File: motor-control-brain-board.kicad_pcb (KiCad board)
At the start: 2 copper layers, 107 parts, among them J1 GPIO, J10 PWM, J11 PWR, J12 POWER_SENSE, J13 MISC_SENSE, J2 I2C, J3 SERIAL_1, J4 SERIAL_2, J5 CAN, J6 SPI, J7 USB_C_Receptacle_USB2.0_16P, J8 SWD, J9 POS_SENSE, SW1 RST, U1 TLV76750QWDRBxQ1, U10 TLV6001DCK, U11 TLV6001DCK, U12 TLV6001DCK, U2 TLV76733QWDRBxQ1, U3 M95256-WMN6P, U4 STM32G474RETx, U5 TCAN1044V-Q1, U6 TLV6001DCK, U7 TLV6001DCK, U8 TLV6001DCK, U9 TLV6001DCK

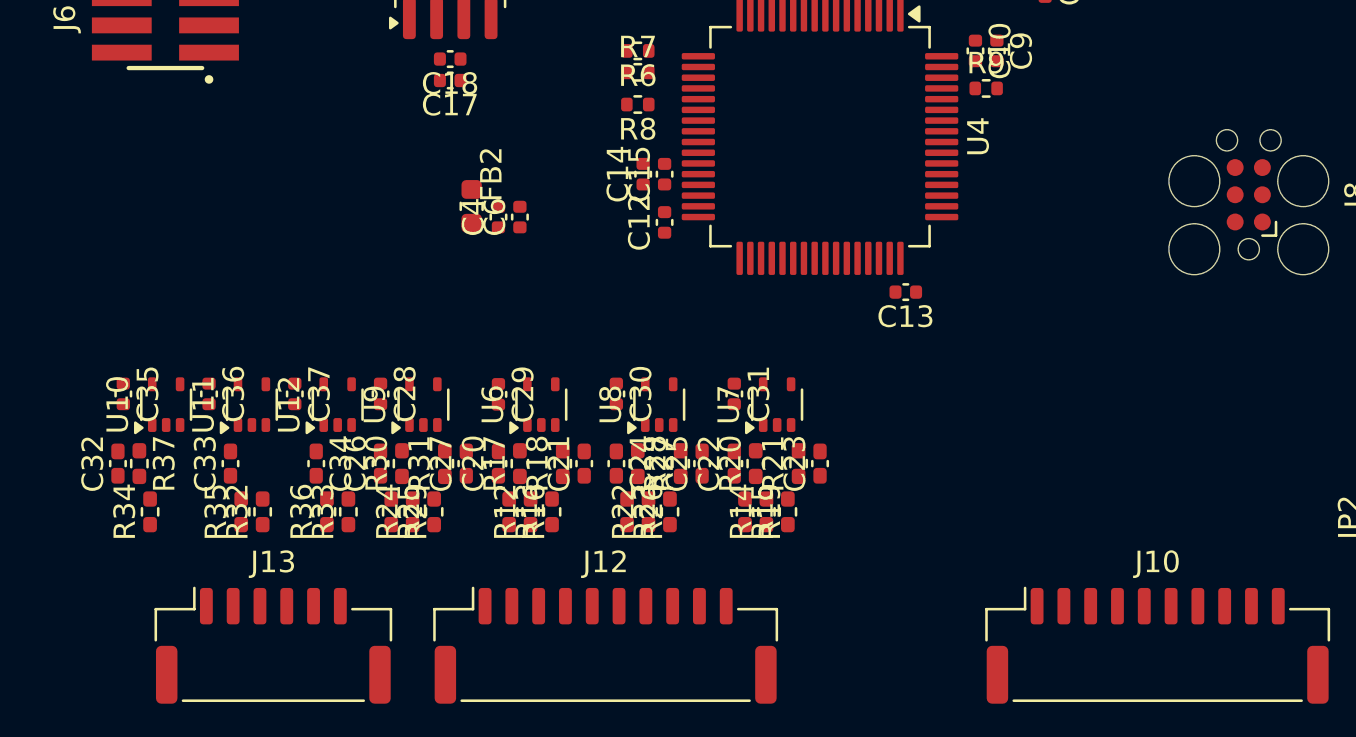
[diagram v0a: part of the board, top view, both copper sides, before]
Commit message: Started routing PCB
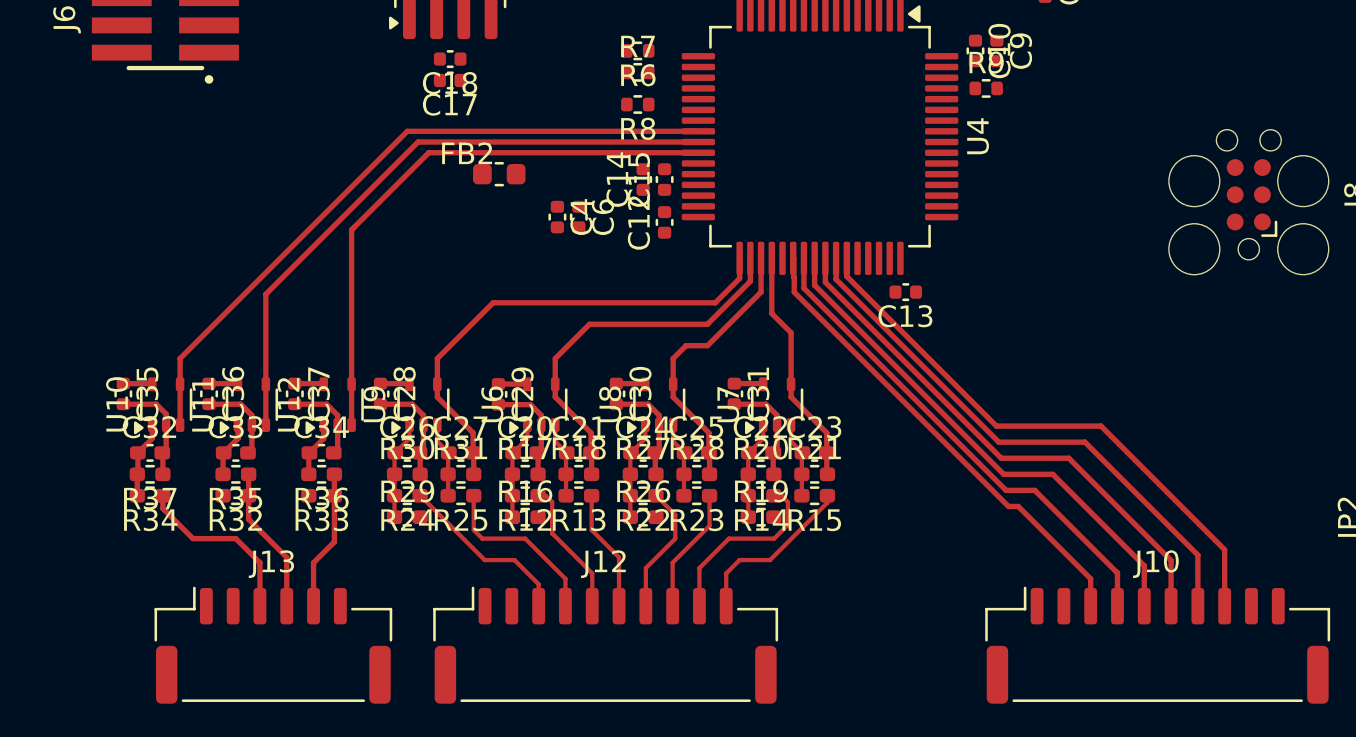
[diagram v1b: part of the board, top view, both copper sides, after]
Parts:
- C19: value C -> 4n7
- moved C4 2.75 mm to (128.0, 102.0), turned to -90 degrees
- moved C6 2.75 mm to (129.0, 102.0), turned to -90 degrees
- moved FB2 1.98 mm to (125.3, 100.0), turned to 0 degrees
- moved R35 1.77 mm to (113.0, 114.0), turned to 180 degrees
- moved R36 1.77 mm to (117.0, 114.0), turned to 180 degrees
- moved C32 1.58 mm to (109.0, 113.0), turned to 0 degrees
- moved R13 1.46 mm to (129.0, 115.0), turned to 180 degrees
- moved R15 1.46 mm to (140.0, 115.0), turned to 180 degrees
- moved R23 1.46 mm to (134.5, 115.0), turned to 180 degrees
- moved R25 1.46 mm to (123.5, 115.0), turned to 180 degrees
- moved R32 1.46 mm to (113.0, 115.0), turned to 180 degrees
- moved R33 1.46 mm to (117.0, 115.0), turned to 180 degrees
- moved C20 1.35 mm to (126.5, 113.0), turned to 0 degrees
- moved C22 1.35 mm to (137.5, 113.0), turned to 0 degrees
- moved C24 1.35 mm to (132.0, 113.0), turned to 0 degrees
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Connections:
- J1 pad 10: /GPIO_7 -> GND
- J1 pad 3: GND -> /GPIO_1
- J1 pad 4: /GPIO_1 -> /GPIO_2
- J1 pad 5: /GPIO_2 -> /GPIO_3
- J1 pad 6: /GPIO_3 -> /GPIO_4
- J1 pad 7: /GPIO_4 -> /GPIO_5
- J1 pad 8: /GPIO_5 -> /GPIO_6
- J1 pad 9: /GPIO_6 -> /GPIO_7
- J10 pad 10: /PWM_EN -> GND
- J10 pad 3: GND -> /PWM_C_H
- J10 pad 4: /PWM_A_HI -> /PWM_C_L
- J10 pad 5: /PWM_B_HI -> /PWM_B_H
- J10 pad 6: /PWM_C_HI -> /PWM_B_L
- J10 pad 7: /PWM_A_LO -> /PWM_A_H
- J10 pad 8: /PWM_B_LO -> /PWM_A_L
- J10 pad 9: /PWM_C_LO -> /PWM_EN
- J12 pad 10: /CURR_C- -> GND
- J12 pad 2: GND -> /VOLT_DC+
- J12 pad 3: /VOLT_DC+ -> /VOLT_DC-
- J12 pad 4: /VOLT_DC- -> /CURR_A+
- J12 pad 5: /CURR_A+ -> /CURR_A-
- J12 pad 6: /CURR_A- -> /CURR_B+
- J12 pad 7: /CURR_B+ -> /CURR_B-
- J12 pad 8: /CURR_B- -> /CURR_C+
- J12 pad 9: /CURR_C+ -> /CURR_C-
- J13 pad 2: GND -> /ACC+
- J13 pad 3: /ACC+ -> /THM_1+
- J13 pad 4: /THM_1+ -> /THM_2+
- J13 pad 5: /THM_2+ -> GND
- J2 pad 2: GND -> /I2C_SDA
- J2 pad 3: /I2C_SDA -> /I2C_SCL
- J2 pad 4: /I2C_SCL -> GND
- J3 pad 2: GND -> /UART1_TX
- J3 pad 4: /UART1_TX -> GND
- J4 pad 2: GND -> /UART2_TX
- J4 pad 4: /UART2_TX -> GND
- J5 pad 2: GND -> /CANH
- J5 pad 3: /CANH -> /CANL
- J5 pad 4: /CANL -> GND
- J9 pad 2: GND -> /POS_A
- J9 pad 3: /POS_A -> /POS_B
- J9 pad 4: /POS_B -> /POS_C/RES_OUT
- J9 pad 5: /POS_C/RES_OUT -> /POS_Z
- J9 pad 6: /POS_Z -> GND
- U4 pad 38: /PWM_A_HI -> /PWM_C_H
- U4 pad 39: /PWM_B_HI -> /PWM_C_L
- U4 pad 40: /PWM_C_HI -> /PWM_B_H
- U4 pad 41: unconnected-(U4-PC9-Pad41) -> /PWM_B_L
- U4 pad 42: /I2C_SDA -> /PWM_A_H
- U4 pad 43: /I2C_SCL -> /PWM_A_L
- U4 pad 51: unconnected-(U4-PA15-Pad51) -> /I2C_SCL
- U4 pad 52: /PWM_A_LO -> unconnected-(U4-PC10-Pad52)
- U4 pad 53: /PWM_B_LO -> unconnected-(U4-PC11-Pad53)
- U4 pad 54: /PWM_C_LO -> unconnected-(U4-PC12-Pad54)
- U4 pad 60: unconnected-(U4-PB7-Pad60) -> /I2C_SDA
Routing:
- net GND: track 0.00 -> 33.4 mm
- net /ACC: track 0.00 -> 31.7 mm
- net /THM_1: track 0.00 -> 29.2 mm
- net /THM_2: track 0.00 -> 26.8 mm
- net /PWM_A_L: track 0.00 -> 26.4 mm
- net /PWM_A_H: track 0.00 -> 25.6 mm
- net /PWM_B_L: track 0.00 -> 24.8 mm
- net /PWM_B_H: track 0.00 -> 23.9 mm
- net /PWM_C_L: track 0.00 -> 23.1 mm
- net /VOLT_DC: track 0.00 -> 22.7 mm
- net /PWM_C_H: track 0.00 -> 22.3 mm
- net /CURR_A: track 0.00 -> 17.8 mm
- net /CURR_B: track 0.00 -> 13.1 mm
- net /CURR_C: track 0.00 -> 11.2 mm
- net +3V3A: track 0.00 -> 9.53 mm
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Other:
- copper layers 2 -> 4

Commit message: Routed Stuff
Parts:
- moved C3 32.3 mm to (160.2, 111.8), turned to 0 degrees
- moved J11 30.0 mm to (166.6, 106.1), turned to 90 degrees
- moved U1 29.0 mm to (161.0, 109.0), turned to -90 degrees
- moved D2 25.9 mm to (158.8, 109.0), turned to 90 degrees
- moved C5 23.6 mm to (160.2, 106.2)
- moved U2 21.8 mm to (161.0, 103.5), turned to -90 degrees
- moved C7 16.3 mm to (160.2, 100.8), turned to 180 degrees
- moved J7 16.1 mm to (166.2, 89.2)
- moved R3 16.1 mm to (160.0, 91.6)
- moved R4 16.1 mm to (160.0, 90.6)
- moved D1 15.2 mm to (159.5, 95.8)
- moved C2 14.2 mm to (159.5, 94.5)
- moved FB1 13.0 mm to (161.2, 97.5)
- moved D3 11.9 mm to (165.2, 100.0)
- moved R5 11.5 mm to (165.2, 98.5)
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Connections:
- J5 pad 2: /CANH -> /CANL
- J5 pad 3: /CANL -> /CANH
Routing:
- net +3V3A: track 9.53 -> 0.00 mm
- net GND: track 33.4 -> 24.0 mm
- net /CANL: track 0.00 -> 8.43 mm
- net /CANH: track 0.00 -> 8.43 mm
- net /PWM_A_L: track 26.4 -> 20.3 mm
- net /PWM_A_H: track 25.6 -> 20.0 mm
- net /PWM_B_L: track 24.8 -> 19.7 mm
- net /PWM_B_H: track 23.9 -> 19.4 mm
- net /PWM_C_L: track 23.1 -> 19.1 mm
- net /PWM_C_H: track 22.3 -> 18.8 mm
- net /MCU/CAN_MID: track 0.00 -> 3.20 mm
- net +5V: track 0.00 -> 2.84 mm
- net /ACC+: track 8.20 -> 5.37 mm
- net /VOLT_DC-: track 8.09 -> 6.20 mm
- net /VOLT_DC+: track 8.26 -> 6.80 mm
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
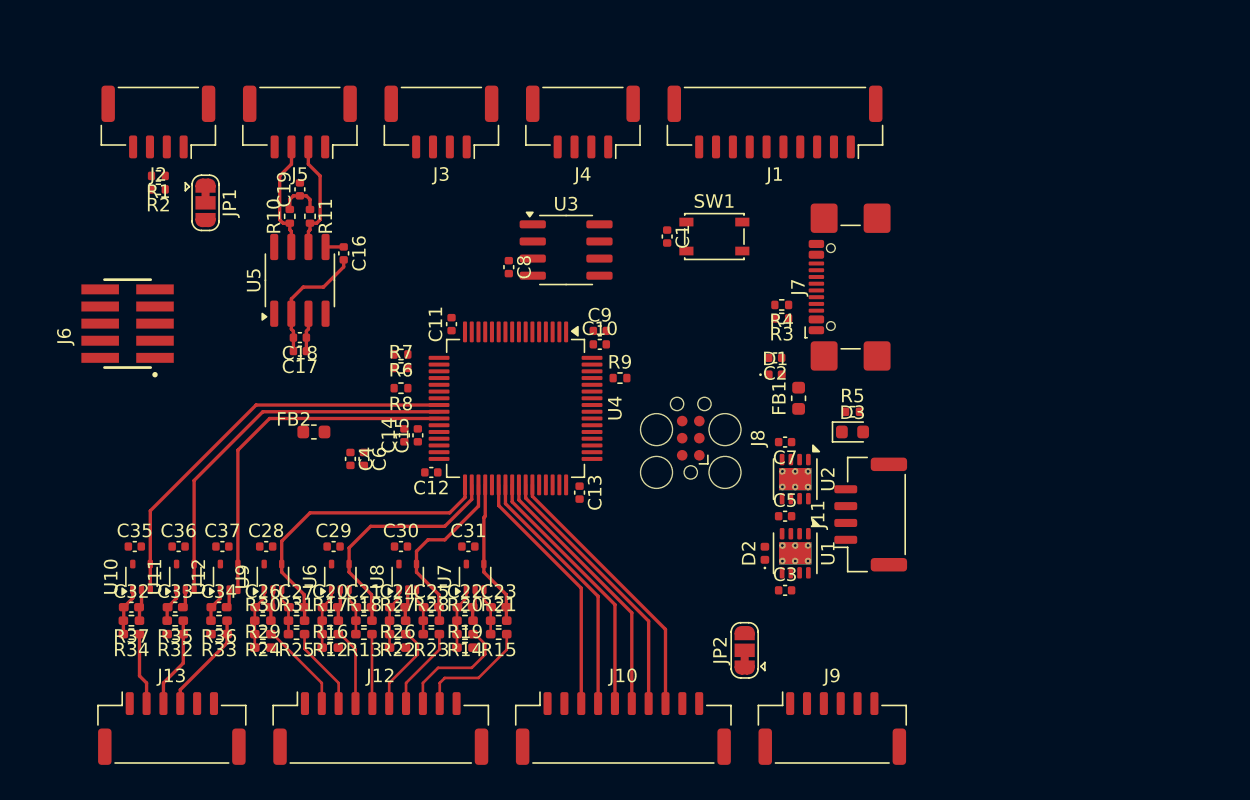
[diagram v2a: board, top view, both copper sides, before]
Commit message: Made board size exactly 50mmx60mm
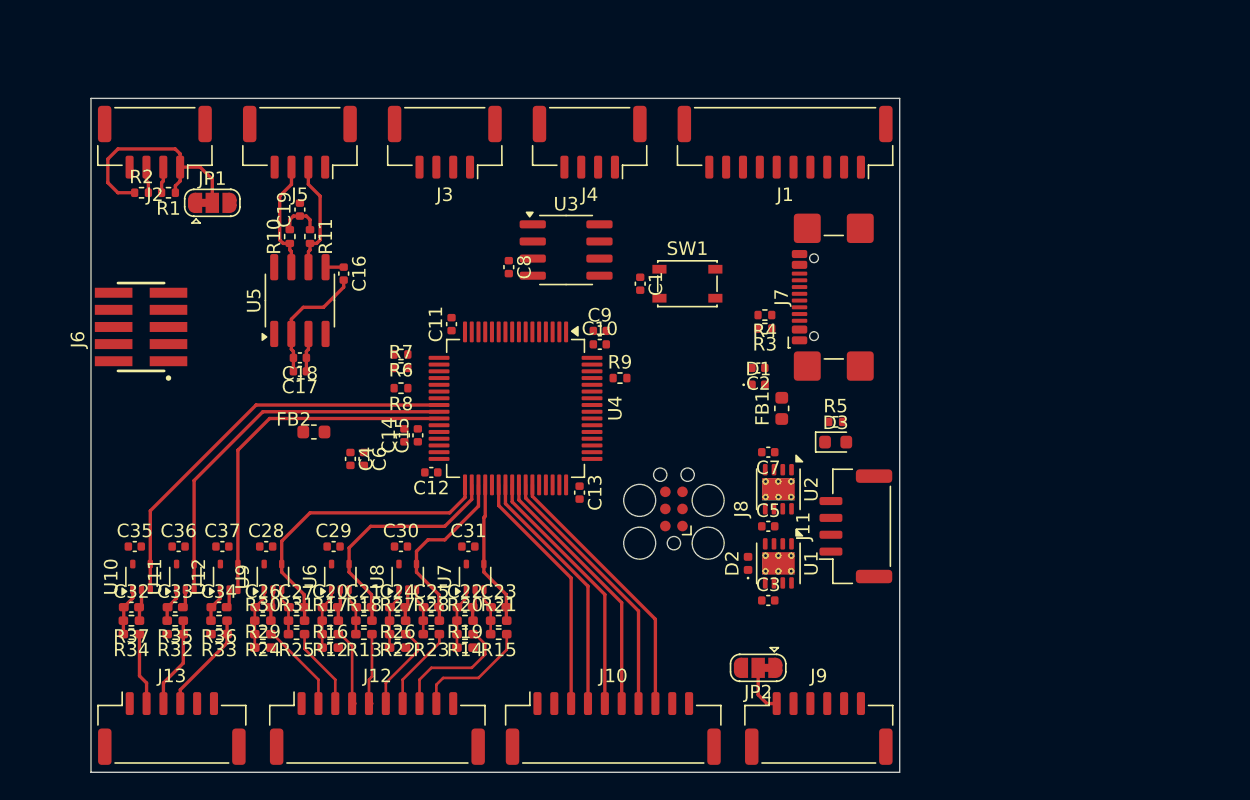
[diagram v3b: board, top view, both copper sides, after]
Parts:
- moved J8 5.40 mm to (152.0, 105.7)
- moved C1 4.03 mm to (149.5, 89.0)
- moved SW1 4.03 mm to (153.0, 89.0)
- moved J1 1.68 mm to (160.2, 78.5)
- moved JP2 1.64 mm to (158.2, 117.5), turned to 180 degrees
- moved J4 1.58 mm to (145.8, 78.5)
- moved J2 1.52 mm to (113.5, 78.5)
- moved J3 1.52 mm to (135.0, 78.5)
- moved C16 1.50 mm to (127.5, 88.2)
- moved C17 1.50 mm to (124.2, 95.5)
- moved C18 1.50 mm to (124.2, 94.5)
- moved C19 1.50 mm to (124.2, 83.5)
- moved J5 1.50 mm to (124.2, 78.5)
- moved R10 1.50 mm to (123.5, 85.5)
- moved R11 1.50 mm to (125.0, 85.5)
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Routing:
- net /PWR_I2C: track 0.00 -> 17.4 mm
- net /PWR_POS: track 0.00 -> 3.64 mm
- net /I2C_SCL: track 0.00 -> 1.96 mm
- net /I2C_SDA: track 0.00 -> 1.95 mm
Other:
- board outline added: 60 x 50 mm

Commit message: Continued work on PCB layout, think I should add castellated holes as an alternative to connectors
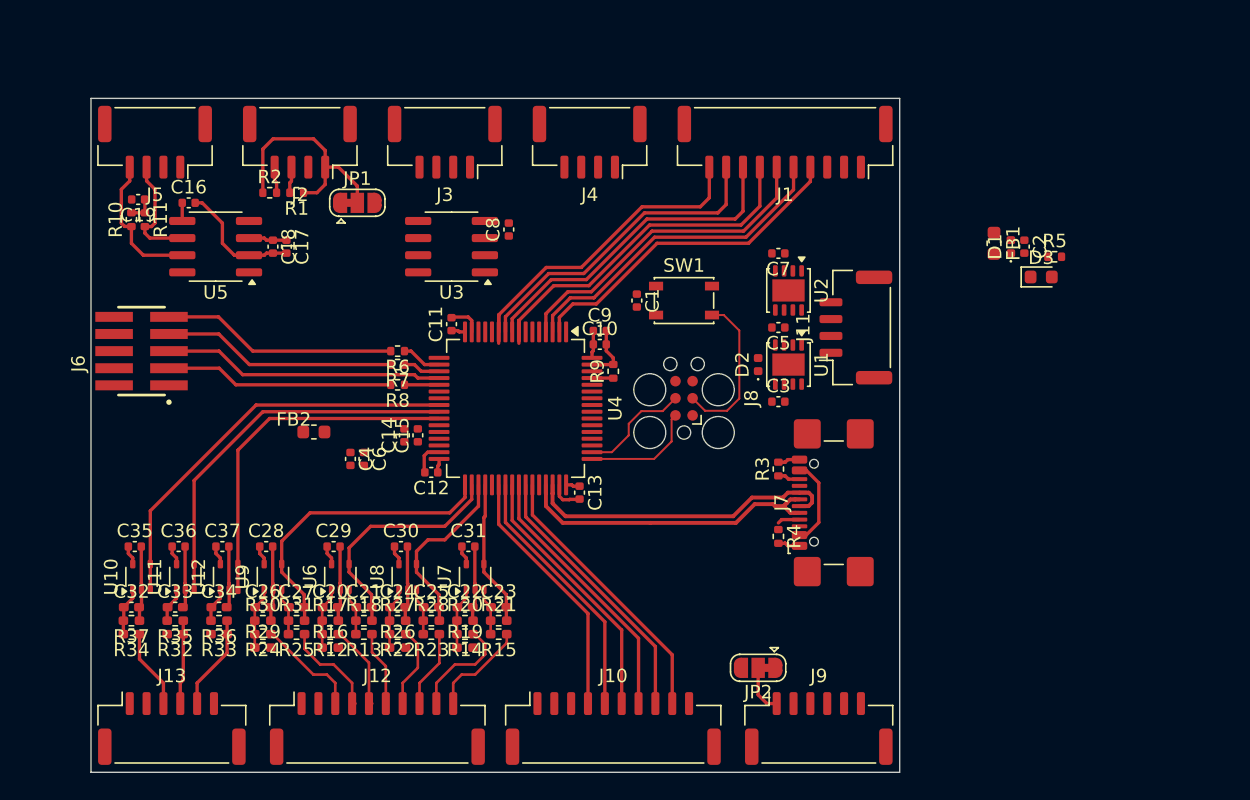
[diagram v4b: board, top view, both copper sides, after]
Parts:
- U1, U2: footprint Package_SON:VSON-8-1EP_3x3mm_P0.65mm_EP1.65x2.4mm_ThermalVias -> Package_SON:VSON-8-1EP_3x3mm_P0.65mm_EP1.65x2.4mm
- moved C2 21.7 mm to (178.0, 86.2), turned to -90 degrees
- moved D1 21.4 mm to (177.0, 86.2), turned to 90 degrees
- moved R5 20.4 mm to (180.2, 87.0)
- moved FB1 20.0 mm to (175.8, 86.0), turned to -90 degrees
- moved D3 19.6 mm to (179.2, 88.5)
- moved R4 16.5 mm to (159.8, 107.8), turned to -90 degrees
- moved J7 15.2 mm to (165.0, 105.2)
- moved C3 14.8 mm to (159.8, 97.8)
- moved C5 14.8 mm to (159.8, 92.2), turned to 180 degrees
- moved C7 14.8 mm to (159.8, 86.8)
- moved D2 14.8 mm to (158.2, 95.0)
- moved U1 14.8 mm to (160.5, 95.0)
- moved U2 14.8 mm to (160.5, 89.5)
- moved J11 14.8 mm to (165.5, 92.2)
- moved C16 12.6 mm to (116.0, 83.0), turned to 0 degrees
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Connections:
- J1 pad 10: GND -> /GPIO_7
- J1 pad 3: /GPIO_1 -> GND
- J1 pad 4: /GPIO_2 -> /GPIO_1
- J1 pad 5: /GPIO_3 -> /GPIO_2
- J1 pad 6: /GPIO_4 -> /GPIO_3
- J1 pad 7: /GPIO_5 -> /GPIO_4
- J1 pad 8: /GPIO_6 -> /GPIO_5
- J1 pad 9: /GPIO_7 -> /GPIO_6
- J10 pad 10: GND -> /PWM_EN
- J10 pad 3: /PWM_C_H -> GND
- J10 pad 4: /PWM_C_L -> /PWM_C_H
- J10 pad 5: /PWM_B_H -> /PWM_C_L
- J10 pad 6: /PWM_B_L -> /PWM_B_H
- J10 pad 7: /PWM_A_H -> /PWM_B_L
- J10 pad 8: /PWM_A_L -> /PWM_A_H
- J10 pad 9: /PWM_EN -> /PWM_A_L
- J12 pad 10: GND -> /CURR_C-
- J12 pad 2: /VOLT_DC+ -> GND
- J12 pad 3: /VOLT_DC- -> /VOLT_DC+
- J12 pad 4: /CURR_A+ -> /VOLT_DC-
- J12 pad 5: /CURR_A- -> /CURR_A+
- J12 pad 6: /CURR_B+ -> /CURR_A-
- J12 pad 7: /CURR_B- -> /CURR_B+
- J12 pad 8: /CURR_C+ -> /CURR_B-
- J12 pad 9: /CURR_C- -> /CURR_C+
- J13 pad 2: /ACC+ -> GND
- J13 pad 3: /THM_1+ -> /ACC+
- J13 pad 4: /THM_2+ -> /THM_1+
- J13 pad 5: GND -> /THM_2+
- J2 pad 2: /I2C_SDA -> GND
- J2 pad 3: /I2C_SCL -> /I2C_SDA
- J2 pad 4: GND -> /I2C_SCL
- J3 pad 2: /UART1_TX -> GND
- J3 pad 3: /UART1_RX -> /UART1_TX
- J3 pad 4: GND -> /UART1_RX
- J4 pad 2: /UART2_TX -> GND
- J4 pad 3: /UART2_RX -> /UART2_TX
- J4 pad 4: GND -> /UART2_RX
- J5 pad 2: /CANL -> GND
- J5 pad 3: /CANH -> /CANL
- J5 pad 4: GND -> /CANH
- J9 pad 2: /POS_A -> GND
- J9 pad 3: /POS_B -> /POS_A
- J9 pad 4: /POS_C/RES_OUT -> /POS_B
- J9 pad 5: /POS_Z -> /POS_C/RES_OUT
- J9 pad 6: GND -> /POS_Z
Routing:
- net GND: track 24.0 -> 61.5 mm
- net /GPIO_4: track 0.00 -> 26.8 mm
- net /GPIO_1: track 0.00 -> 24.9 mm
- net /GPIO_7: track 0.00 -> 24.9 mm
- net /GPIO_5: track 0.00 -> 24.7 mm
- net /GPIO_2: track 0.00 -> 24.6 mm
- net /GPIO_3: track 0.00 -> 24.3 mm
- net /GPIO_6: track 0.00 -> 23.7 mm
- net /USB_D-: track 0.00 -> 23.4 mm
- net /USB_D+: track 0.00 -> 23.4 mm
- net /SPI_MISO: track 0.00 -> 20.9 mm
- net /SPI_NSS: track 0.00 -> 17.5 mm
- net /SPI_SCK: track 0.00 -> 17.4 mm
- net /SPI_MOSI: track 0.00 -> 17.0 mm
- net /NRST: track 0.00 -> 11.8 mm
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
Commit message: Moved connectors for IO to 'external' edges and connectors for inverter to 'interior' edges
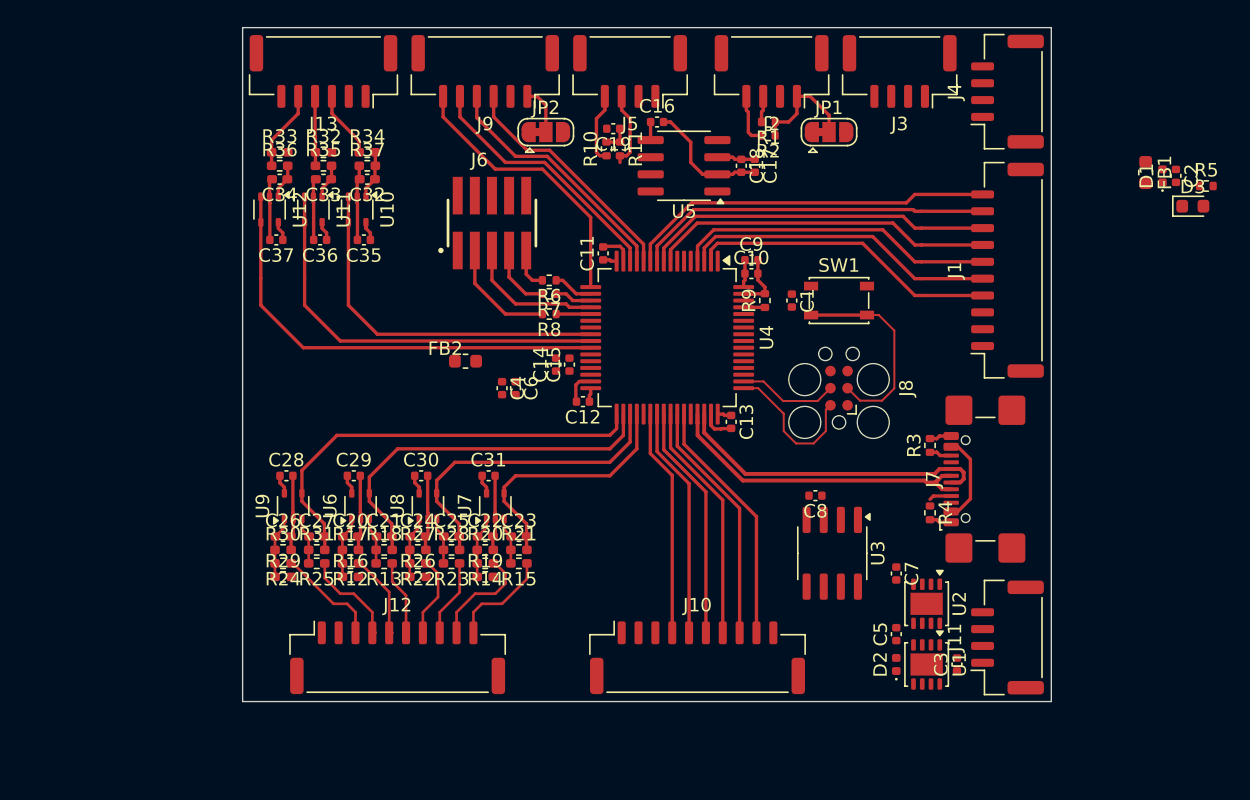
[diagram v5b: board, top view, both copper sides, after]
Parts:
- moved J9 54.7 mm to (138.0, 73.2), turned to 180 degrees
- moved J13 50.0 mm to (126.0, 73.2), turned to 180 degrees
- moved JP2 42.8 mm to (142.5, 77.8), turned to 0 degrees
- moved R34 39.8 mm to (129.2, 79.2), turned to 0 degrees
- moved R37 38.0 mm to (129.2, 80.2), turned to 0 degrees
- moved R32 37.4 mm to (126.0, 79.2), turned to 0 degrees
- moved R2 37.2 mm to (159.0, 78.0), turned to 180 degrees
- moved U3 36.3 mm to (163.8, 109.0), turned to -90 degrees
- moved C32 36.3 mm to (129.2, 81.2), turned to 180 degrees
- moved R33 36.0 mm to (122.8, 79.2), turned to 0 degrees
- moved C19 35.6 mm to (147.5, 77.5)
- moved J5 35.6 mm to (148.8, 73.2)
- moved R10 35.6 mm to (147.0, 79.0)
- moved R11 35.6 mm to (148.0, 79.0)
- moved R35 35.5 mm to (126.0, 80.2), turned to 0 degrees
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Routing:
- net /POS_Z: track 0.00 -> 20.7 mm
- net /POS_C/RES_OUT: track 0.00 -> 19.2 mm
- net /POS_B: track 0.00 -> 18.5 mm
- net /POS_A: track 0.00 -> 17.8 mm
- net /SPI_NSS: track 17.5 -> 3.15 mm
- net /SPI_SCK: track 17.4 -> 4.98 mm
- net /SPI_MISO: track 20.9 -> 10.4 mm
- net /CURR_B: track 13.4 -> 23.5 mm
- net /CURR_A: track 17.8 -> 27.8 mm
- net /VOLT_DC: track 22.5 -> 32.3 mm
- net /PWR_I2C: track 17.1 -> 8.36 mm
- net /SPI_MOSI: track 17.0 -> 8.40 mm
- net /CURR_C: track 10.8 -> 19.0 mm
- net /THM_2: track 26.2 -> 33.8 mm
- net /CANH: track 10.6 -> 5.27 mm
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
